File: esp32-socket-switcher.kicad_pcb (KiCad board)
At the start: 4 copper layers, 49.8 x 34.5 mm, 45 parts, among them IC1 ADP2301AUJZ-R7, J1 USB4110GFA, J2 4DB-P108-06, K1 G5CA-1A DC5, Q1 SS8050-G, Q2 SS8050-G, Q3 CSD17575Q3T, U2 ESP32-WROOM-32E-H4, U5 CP2102N-A02-GQFN24R

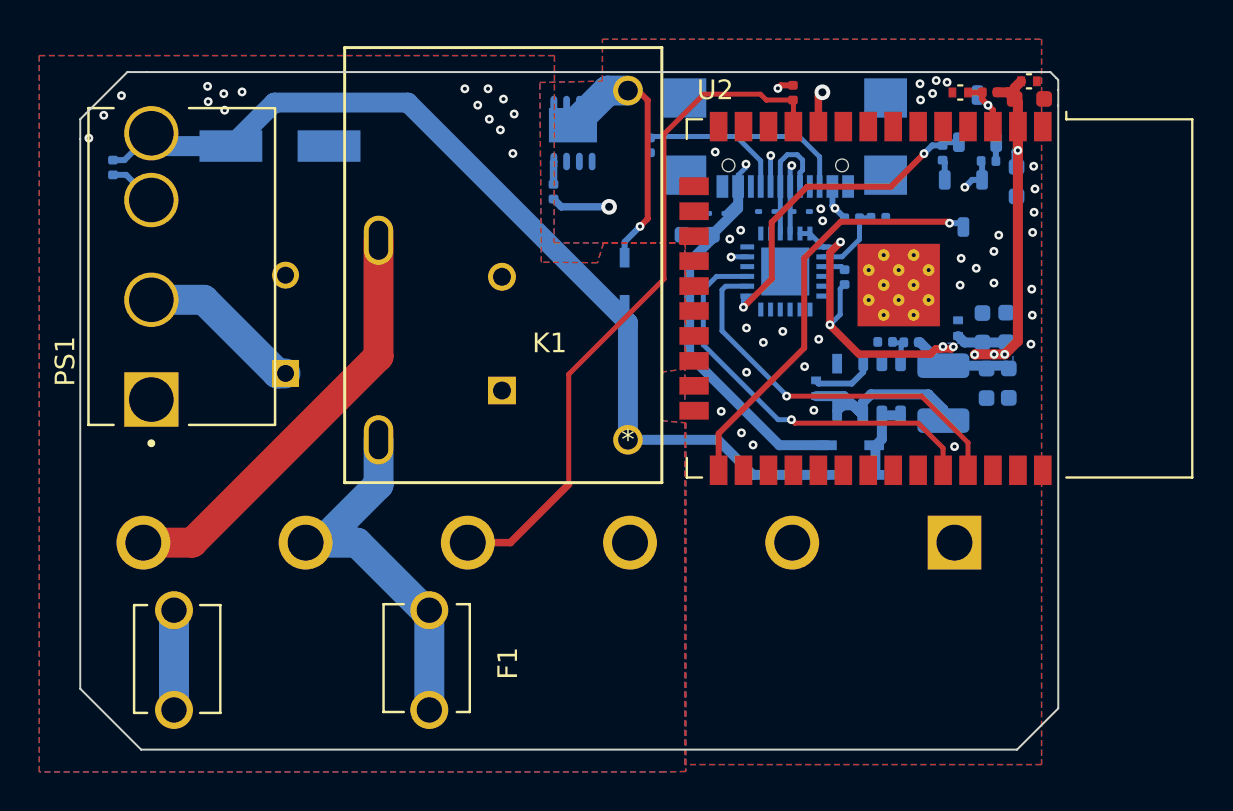
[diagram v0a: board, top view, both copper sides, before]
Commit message: updated usbc connector to one that's ACTUALLY FUCKING IN STOCK
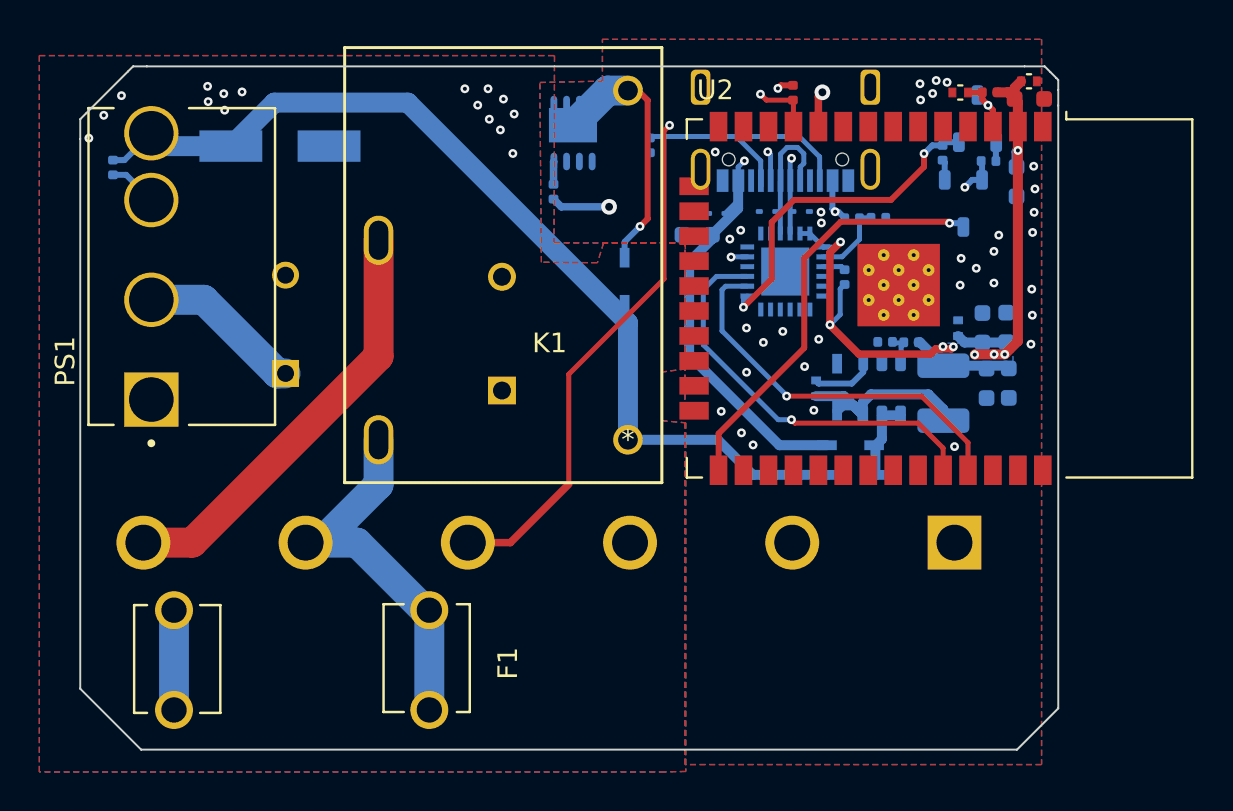
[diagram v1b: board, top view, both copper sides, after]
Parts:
- removed J1: USB4110GFA, esp32-socket-switcher:GCT_USB4110GFA
- added J3: USB4105-GF-A, esp32-socket-switcher:GCT_USB4105-GF-A, B.Cu at (90.8, 42.5)
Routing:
- net /D-: track 6.35 -> 7.03 mm
- net /VUSB: track 29.5 -> 30.1 mm
- net /D+: track 6.45 -> 6.95 mm
- net /SWITCH_IN: track 35.1 -> 35.2 mm, vias 0 -> 2
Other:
- board size 49.8 x 34.5 mm -> 49.8 x 34.8 mm

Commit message: teardrops and curvy traces
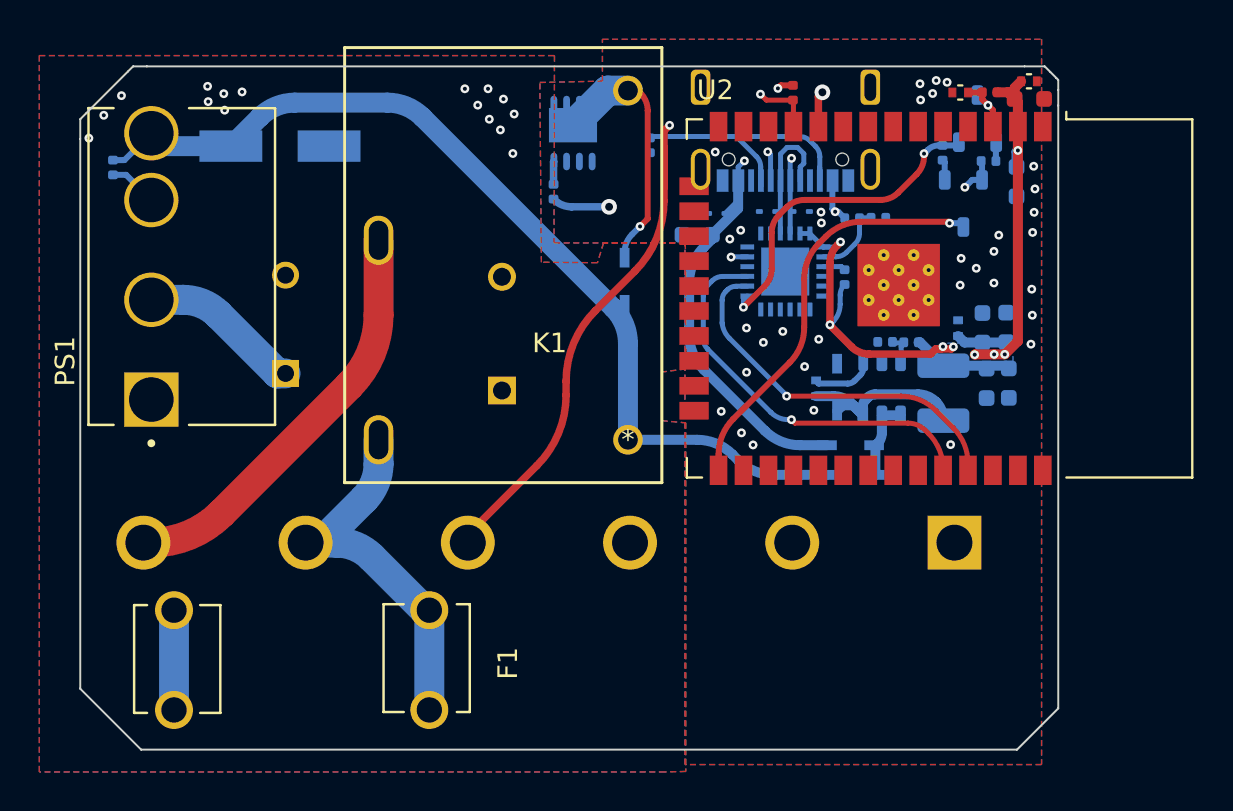
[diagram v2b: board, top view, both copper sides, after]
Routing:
- net Net-(J3-CC1): track 13.4 -> 14.2 mm
- net /SWITCH_IN: track 35.2 -> 35.9 mm
- net /VDC-WALL: track 49.5 -> 48.9 mm
- net Net-(F1-Pad2): track 31.9 -> 31.3 mm
- net /ESP32/CP210x_RX: track 19.8 -> 19.2 mm
